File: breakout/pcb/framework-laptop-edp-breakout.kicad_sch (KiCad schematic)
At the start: 7 parts, among them J1 20879-040E-01, J2 Conn_01x40, J3 Conn_01x01

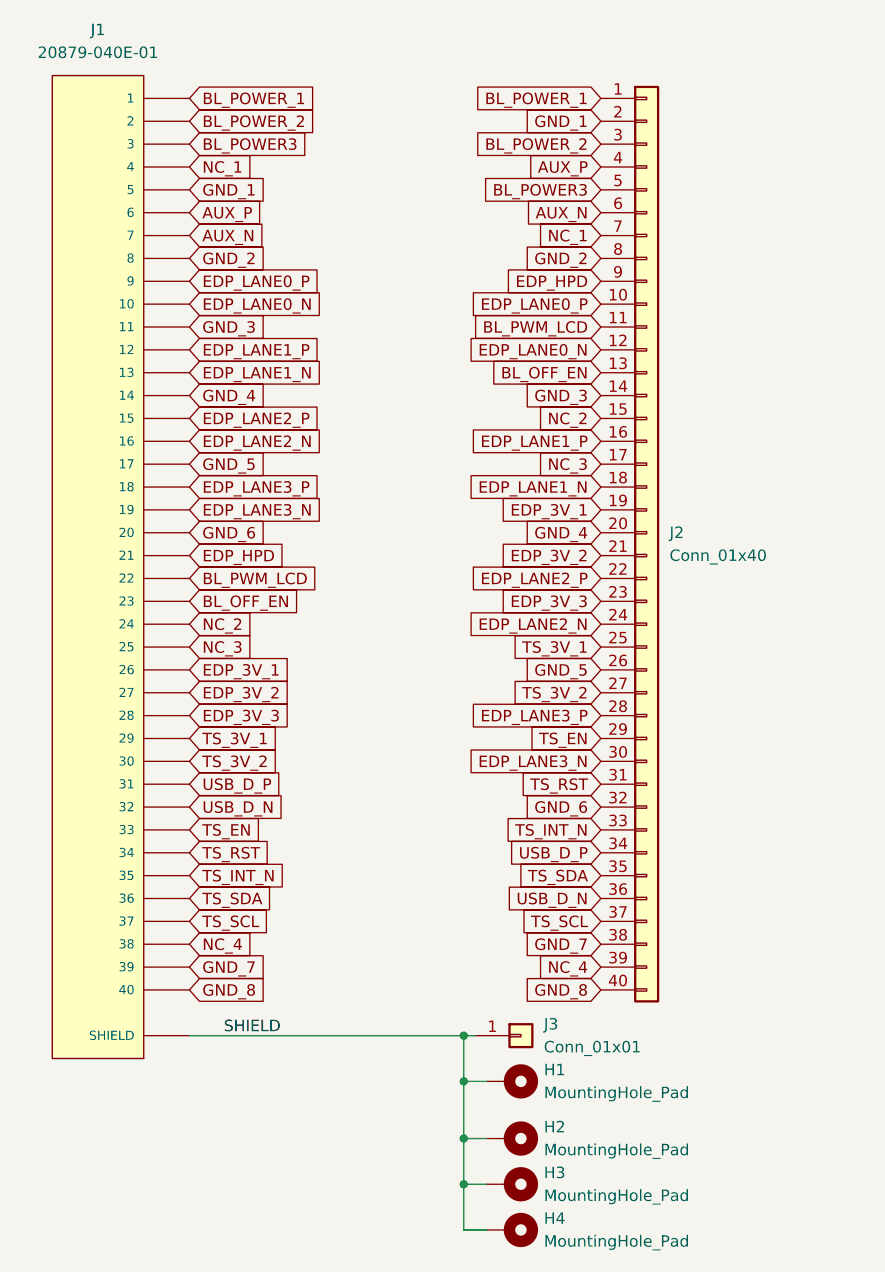
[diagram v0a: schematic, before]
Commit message: rework breakout because pins were wrong
turns out pin out documentation from framework is reversed - pin 40  in pinouts.md is pin 1 on the data sheet for the ipex connector
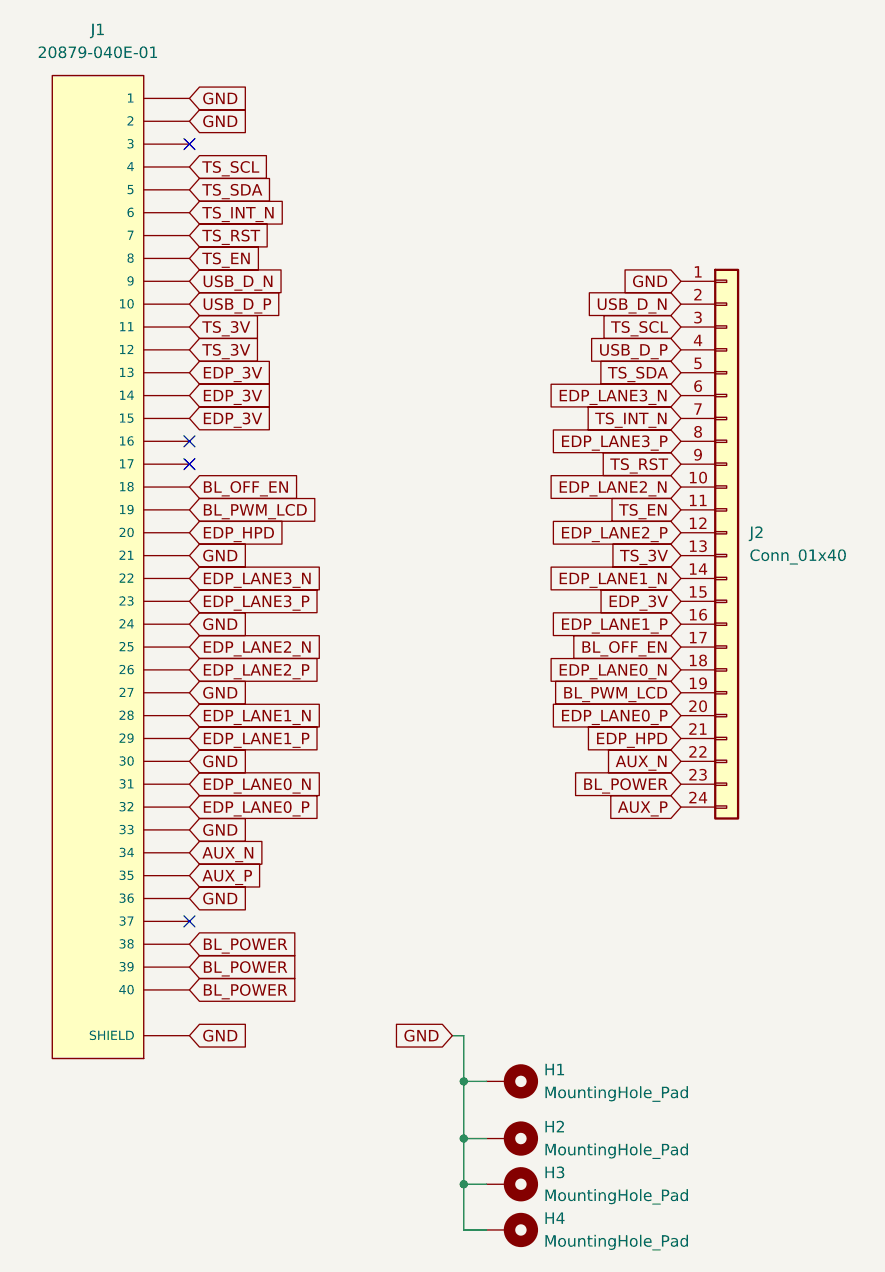
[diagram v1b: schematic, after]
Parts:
- removed J3: Conn_01x01, Connector_PinSocket_2.00mm:PinSocket_1x01_P2.00mm_Vertical, symbol Connector_Generic:Conn_01x01
- J2: footprint Connector_PinSocket_2.00mm:PinSocket_2x20_P2.00mm_Vertical -> Connector_PinSocket_2.54mm:PinSocket_2x12_P2.54mm_Vertical; symbol Connector_Generic:Conn_01x40 -> Connector_Generic:Conn_01x24
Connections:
- net SHIELD is gone; now on net GND: H1.1, H2.1, H3.1, H4.1, J1.S1 (SHIELD), J1.S10 (SHIELD), J1.S11 (SHIELD), J1.S12 (SHIELD), J1.S13 (SHIELD), J1.S14 (SHIELD), J1.S15 (SHIELD), J1.S16 (SHIELD), J1.S17 (SHIELD), J1.S18 (SHIELD), J1.S19 (SHIELD), J1.S2 (SHIELD), J1.S20 (SHIELD), J1.S21 (SHIELD), J1.S22 (SHIELD), J1.S23 (SHIELD), J1.S24 (SHIELD), J1.S25 (SHIELD), J1.S26 (SHIELD), J1.S27 (SHIELD), J1.S28 (SHIELD), J1.S29 (SHIELD), J1.S3 (SHIELD), J1.S30 (SHIELD), J1.S31 (SHIELD), J1.S32 (SHIELD), J1.S33 (SHIELD), J1.S34 (SHIELD), J1.S4 (SHIELD), J1.S5 (SHIELD), J1.S6 (SHIELD), J1.S7 (SHIELD), J1.S8 (SHIELD), J1.S9 (SHIELD)
- net AUX_N: now also J1.34, J2.22 (Pin_22); no longer J1.7, J2.6 (Pin_6)
- net AUX_P: now also J1.35, J2.24 (Pin_24); no longer J1.6, J2.4 (Pin_4)
- net BL_OFF_EN: now also J1.18, J2.17 (Pin_17); no longer J1.23, J2.13 (Pin_13)
- net BL_PWM_LCD: now also J1.19, J2.19 (Pin_19); no longer J1.22, J2.11 (Pin_11)
- net EDP_HPD: now also J1.20, J2.21 (Pin_21); no longer J1.21, J2.9 (Pin_9)
- net EDP_LANE0_N: now also J1.31, J2.18 (Pin_18); no longer J1.10, J2.12 (Pin_12)
- net EDP_LANE0_P: now also J1.32, J2.20 (Pin_20); no longer J1.9, J2.10 (Pin_10)
- net EDP_LANE1_N: now also J1.28, J2.14 (Pin_14); no longer J1.13, J2.18 (Pin_18)
- net EDP_LANE1_P: now also J1.29; no longer J1.12
- net EDP_LANE2_N: now also J1.25, J2.10 (Pin_10); no longer J1.16, J2.24 (Pin_24)
- net EDP_LANE2_P: now also J1.26, J2.12 (Pin_12); no longer J1.15, J2.22 (Pin_22)
- net EDP_LANE3_N: now also J1.22, J2.6 (Pin_6); no longer J1.19, J2.30 (Pin_30)
- net EDP_LANE3_P: now also J1.23, J2.8 (Pin_8); no longer J1.18, J2.28 (Pin_28)
- net TS_EN: now also J1.8, J2.11 (Pin_11); no longer J1.33, J2.29 (Pin_29)
- net TS_INT_N: now also J1.6, J2.7 (Pin_7); no longer J1.35, J2.33 (Pin_33)
- net TS_RST: now also J1.7, J2.9 (Pin_9); no longer J1.34, J2.31 (Pin_31)
- net TS_SCL: now also J1.4, J2.3 (Pin_3); no longer J1.37, J2.37 (Pin_37)
- net TS_SDA: now also J1.5, J2.5 (Pin_5); no longer J1.36, J2.35 (Pin_35)
- net USB_D_N: now also J1.9, J2.2 (Pin_2); no longer J1.32, J2.36 (Pin_36)
- net USB_D_P: now also J1.10, J2.4 (Pin_4); no longer J1.31, J2.34 (Pin_34)
- net BL_POWER3: no longer names the net of J1.3
- net BL_POWER3: no longer J2.5 (Pin_5)
- net BL_POWER_1 renamed GND
- net GND: now also J1.2, J1.21, J1.24, J1.27, J1.30, J1.33, J1.36
- removed net BL_POWER_2: J1.2, J2.3 (Pin_3)
- removed net EDP_3V_1: J1.26, J2.19 (Pin_19)
- removed net EDP_3V_2: J1.27, J2.21 (Pin_21)
- net EDP_3V_3 renamed BL_POWER
- net BL_POWER: now also J1.38, J1.39, J1.40; no longer J1.28
- removed net GND_1: J1.5, J2.2 (Pin_2)
- removed net GND_2: J1.8, J2.8 (Pin_8)
- net GND_3 renamed TS_3V
- net TS_3V: now also J1.12, J2.13 (Pin_13); no longer J2.14 (Pin_14)
- net GND_4 renamed EDP_3V
- net EDP_3V: now also J1.13, J1.15, J2.15 (Pin_15); no longer J2.20 (Pin_20)
- net GND_5: no longer names the net of J1.17
- net GND_5: no longer J2.26 (Pin_26)
- removed net GND_6: J1.20, J2.32 (Pin_32)
- removed net GND_7: J1.39, J2.38 (Pin_38)
- removed net GND_8: J1.40, J2.40 (Pin_40)
- removed net NC_1: J1.4, J2.7 (Pin_7)
- removed net NC_2: J1.24, J2.15 (Pin_15)
- removed net NC_3: J1.25, J2.17 (Pin_17)
- removed net NC_4: J1.38, J2.39 (Pin_39)
- removed net TS_3V_1: J1.29, J2.25 (Pin_25)
- removed net TS_3V_2: J1.30, J2.27 (Pin_27)
- no-connect marks 0 -> 4

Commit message: make breakout use the bundled cable
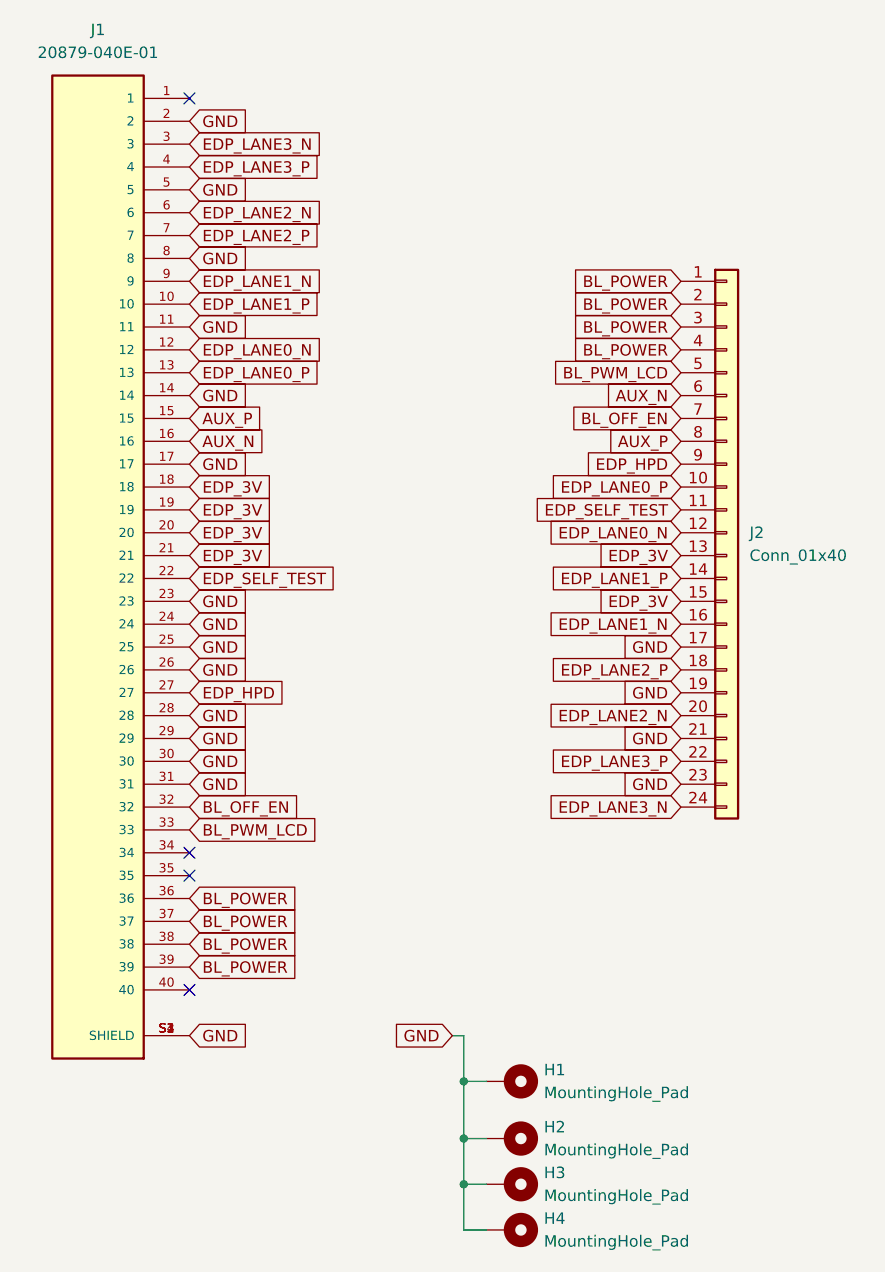
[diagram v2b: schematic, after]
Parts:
- J1: footprint IPEX_20879-040E-01 -> IPEX_20455-040E-76; symbol 20879-040E-01:20879-040E-01 -> 20455-040E-76:20455-040E-76; STANDARD Manufacturer recommendations -> Manufacturer Recommendations
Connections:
- net AUX_N: now also J1.16, J2.6 (Pin_6); no longer J1.34, J2.22 (Pin_22)
- net AUX_P: now also J1.15, J2.8 (Pin_8); no longer J1.35, J2.24 (Pin_24)
- net BL_OFF_EN: now also J1.32, J2.7 (Pin_7); no longer J1.18, J2.17 (Pin_17)
- net BL_POWER: now also J1.36, J1.37, J2.1 (Pin_1), J2.2 (Pin_2), J2.3 (Pin_3), J2.4 (Pin_4); no longer J1.40, J2.23 (Pin_23)
- net BL_PWM_LCD: now also J1.33, J2.5 (Pin_5); no longer J1.19, J2.19 (Pin_19)
- net EDP_3V: now also J1.18, J1.19, J1.20, J1.21, J2.13 (Pin_13); no longer J1.13, J1.14, J1.15
- net EDP_HPD: now also J1.27, J2.9 (Pin_9); no longer J1.20, J2.21 (Pin_21)
- net EDP_LANE0_N: now also J1.12, J2.12 (Pin_12); no longer J1.31, J2.18 (Pin_18)
- net EDP_LANE0_P: now also J1.13, J2.10 (Pin_10); no longer J1.32, J2.20 (Pin_20)
- net EDP_LANE1_N: now also J1.9, J2.16 (Pin_16); no longer J1.28, J2.14 (Pin_14)
- net EDP_LANE1_P: now also J1.10, J2.14 (Pin_14); no longer J1.29, J2.16 (Pin_16)
- net EDP_LANE2_N: now also J1.6, J2.20 (Pin_20); no longer J1.25, J2.10 (Pin_10)
- net EDP_LANE2_P: now also J1.7, J2.18 (Pin_18); no longer J1.26, J2.12 (Pin_12)
- net EDP_LANE3_N: now also J1.3, J2.24 (Pin_24); no longer J1.22, J2.6 (Pin_6)
- net EDP_LANE3_P: now also J1.4, J2.22 (Pin_22); no longer J1.23, J2.8 (Pin_8)
- net GND: now also J1.11, J1.14, J1.17, J1.23, J1.25, J1.26, J1.28, J1.29, J1.31, J1.5, J1.8, J2.17 (Pin_17), J2.19 (Pin_19), J2.21 (Pin_21), J2.23 (Pin_23); no longer J1.1, J1.21, J1.27, J1.33, J1.36, J1.S10 (SHIELD), J1.S11 (SHIELD), J1.S12 (SHIELD), J1.S13 (SHIELD), J1.S14 (SHIELD), J1.S15 (SHIELD), J1.S16 (SHIELD), J1.S17 (SHIELD), J1.S18 (SHIELD), J1.S19 (SHIELD), J1.S20 (SHIELD), J1.S21 (SHIELD), J1.S22 (SHIELD), J1.S23 (SHIELD), J1.S24 (SHIELD), J1.S25 (SHIELD), J1.S26 (SHIELD), J1.S27 (SHIELD), J1.S28 (SHIELD), J1.S29 (SHIELD), J1.S30 (SHIELD), J1.S31 (SHIELD), J1.S32 (SHIELD), J1.S33 (SHIELD), J1.S34 (SHIELD), J1.S5 (SHIELD), J1.S6 (SHIELD), J1.S7 (SHIELD), J1.S8 (SHIELD), J1.S9 (SHIELD), J2.1 (Pin_1)
- removed net TS_3V: J1.11, J1.12, J2.13 (Pin_13)
- net TS_EN renamed EDP_SELF_TEST
- net EDP_SELF_TEST: now also J1.22; no longer J1.8
- removed net TS_INT_N: J1.6, J2.7 (Pin_7)
- removed net TS_RST: J1.7, J2.9 (Pin_9)
- removed net TS_SCL: J1.4, J2.3 (Pin_3)
- removed net TS_SDA: J1.5, J2.5 (Pin_5)
- removed net USB_D_N: J1.9, J2.2 (Pin_2)
- removed net USB_D_P: J1.10, J2.4 (Pin_4)

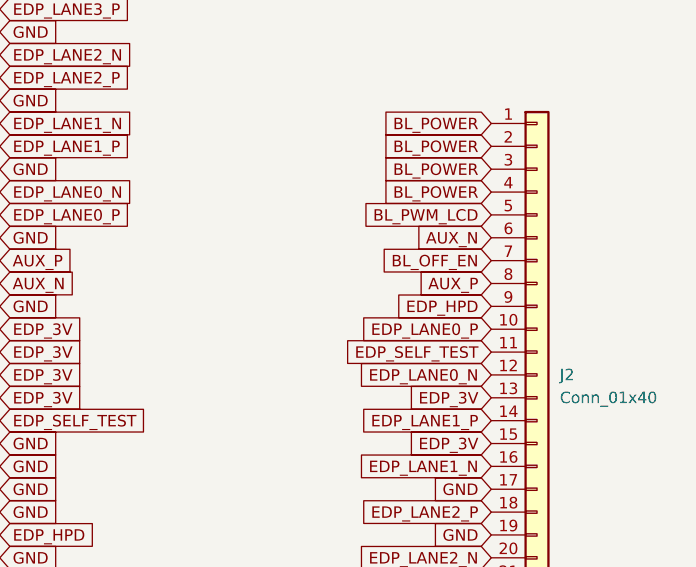
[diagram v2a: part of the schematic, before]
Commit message: migrate breakout to new connector I guess
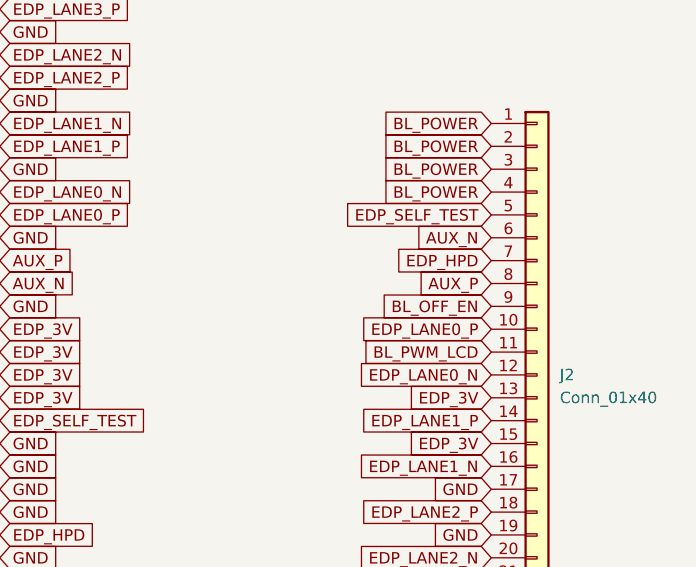
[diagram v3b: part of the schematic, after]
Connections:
- net BL_OFF_EN: now also J2.9 (Pin_9); no longer J2.7 (Pin_7)
- net BL_PWM_LCD: now also J2.11 (Pin_11); no longer J2.5 (Pin_5)
- net EDP_HPD: now also J2.7 (Pin_7); no longer J2.9 (Pin_9)
- net EDP_SELF_TEST: now also J2.5 (Pin_5); no longer J2.11 (Pin_11)
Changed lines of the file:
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@@
-    )
-  )
-  (global_label "EDP_SELF_TEST" (shape input) (at 146.05 78.74 180) (fields_autoplaced)
-    (effects (font (size 1.27 1.27)) (justify right))
-    (property "Intersheet References" "${INTERSHEET_REFS}" (id 0) (at 129.2436 78.8194 0)
-      (effects (font (size 1.27 1.27)) (justify right) hide)
     )
   )
@@
     )
   )
+  (global_label "BL_PWM_LCD" (shape input) (at 146.05 78.74 180) (fields_autoplaced)
+    (effects (font (size 1.27 1.27)) (justify right))
+    (property "Intersheet References" "${INTERSHEET_REFS}" (id 0) (at 131.6626 78.8194 0)
+      (effects (font (size 1.27 1.27)) (justify right) hide)
+    )
+  )
   (global_label "EDP_SELF_TEST" (shape input) (at 91.44 86.36 0) (fields_autoplaced)
     (effects (font (size 1.27 1.27)) (justify left))
@@
     )
   )
-  (global_label "BL_PWM_LCD" (shape input) (at 146.05 63.5 180) (fields_autoplaced)
-    (effects (font (size 1.27 1.27)) (justify right))
-    (property "Intersheet References" "${INTERSHEET_REFS}" (id 0) (at 131.6626 63.5794 0)
-      (effects (font (size 1.27 1.27)) (justify right) hide)
-    )
-  )
   (global_label "GND" (shape input) (at 91.44 66.04 0) (fields_autoplaced)
     (effects (font (size 1.27 1.27)) (justify left))
@@
     )
   )
+  (global_label "BL_OFF_EN" (shape input) (at 146.05 73.66 180) (fields_autoplaced)
+    (effects (font (size 1.27 1.27)) (justify right))
+    (property "Intersheet References" "${INTERSHEET_REFS}" (id 0) (at 133.4164 73.7394 0)
+      (effects (font (size 1.27 1.27)) (justify right) hide)
+    )
+  )
   (global_label "GND" (shape input) (at 91.44 93.98 0) (fields_autoplaced)
     (effects (font (size 1.27 1.27)) (justify left))
@@
     )
   )
+  (global_label "EDP_HPD" (shape input) (at 146.05 68.58 180) (fields_autoplaced)
+    (effects (font (size 1.27 1.27)) (justify right))
+    (property "Intersheet References" "${INTERSHEET_REFS}" (id 0) (at 135.1098 68.6594 0)
+      (effects (font (size 1.27 1.27)) (justify right) hide)
+    )
+  )
   (global_label "GND" (shape input) (at 91.44 106.68 0) (fields_autoplaced)
     (effects (font (size 1.27 1.27)) (justify left))
@@
     )
   )
-  (global_label "EDP_HPD" (shape input) (at 146.05 73.66 180) (fields_autoplaced)
-    (effects (font (size 1.27 1.27)) (justify right))
-    (property "Intersheet References" "${INTERSHEET_REFS}" (id 0) (at 135.1098 73.7394 0)
-      (effects (font (size 1.27 1.27)) (justify right) hide)
-    )
-  )
   (global_label "GND" (shape input) (at 91.44 137.16 0) (fields_autoplaced)
     (effects (font (size 1.27 1.27)) (justify left))
@@
     )
   )
-  (global_label "BL_OFF_EN" (shape input) (at 146.05 68.58 180) (fields_autoplaced)
-    (effects (font (size 1.27 1.27)) (justify right))
-    (property "Intersheet References" "${INTERSHEET_REFS}" (id 0) (at 133.4164 68.6594 0)
-      (effects (font (size 1.27 1.27)) (justify right) hide)
-    )
-  )
   (global_label "GND" (shape input) (at 120.65 137.16 180) (fields_autoplaced)
     (effects (font (size 1.27 1.27)) (justify right))
@@
     )
   )
+  (global_label "EDP_SELF_TEST" (shape input) (at 146.05 63.5 180) (fields_autoplaced)
+    (effects (font (size 1.27 1.27)) (justify right))
+    (property "Intersheet References" "${INTERSHEET_REFS}" (id 0) (at 129.2436 63.5794 0)
+      (effects (font (size 1.27 1.27)) (justify right) hide)
+    )
+  )
